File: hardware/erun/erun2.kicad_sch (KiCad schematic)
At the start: 21 parts, among them J1 Conn_Coaxial, J10 Conn_01x03_Female, J2 HEIDENHAIN_MT25_TTL, J3 TRIGGER_TTL, J4 Conn_01x02_Female, J5 Conn_01x02_Female, J6 Conn_01x02_Female, J7 Conn_01x02_Female, J8 Conn_01x02_Female, J9 Conn_01x03_Female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

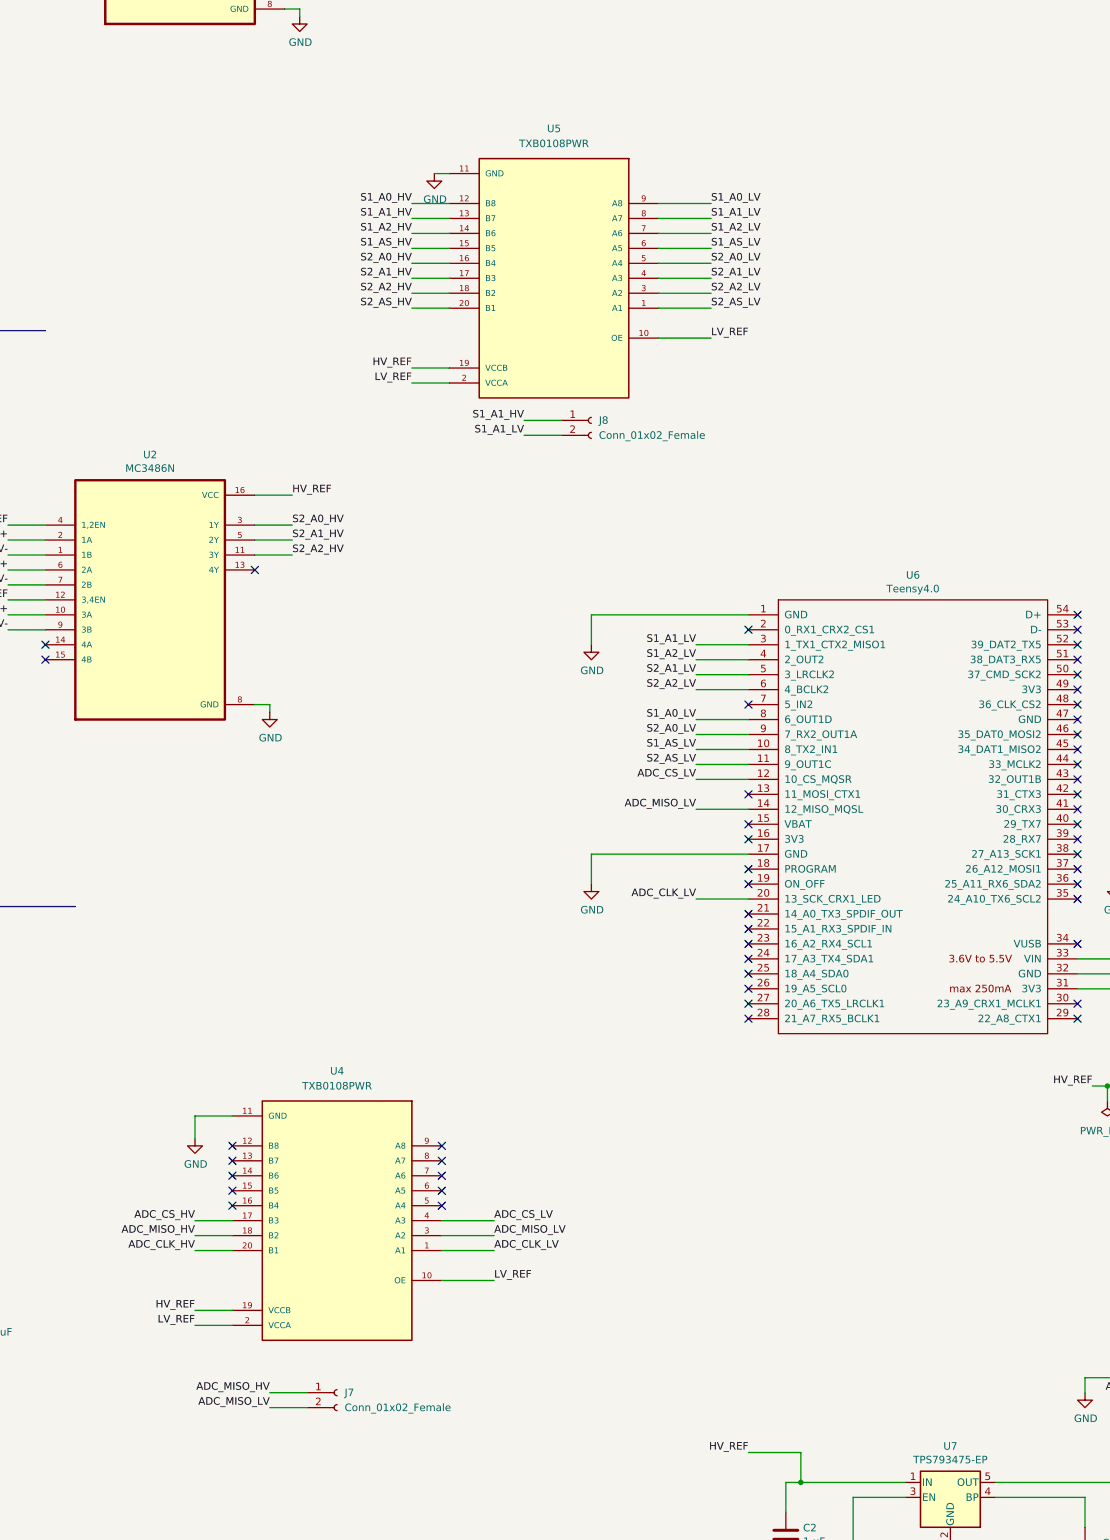
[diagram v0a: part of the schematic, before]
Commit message: Added capacitors to the board
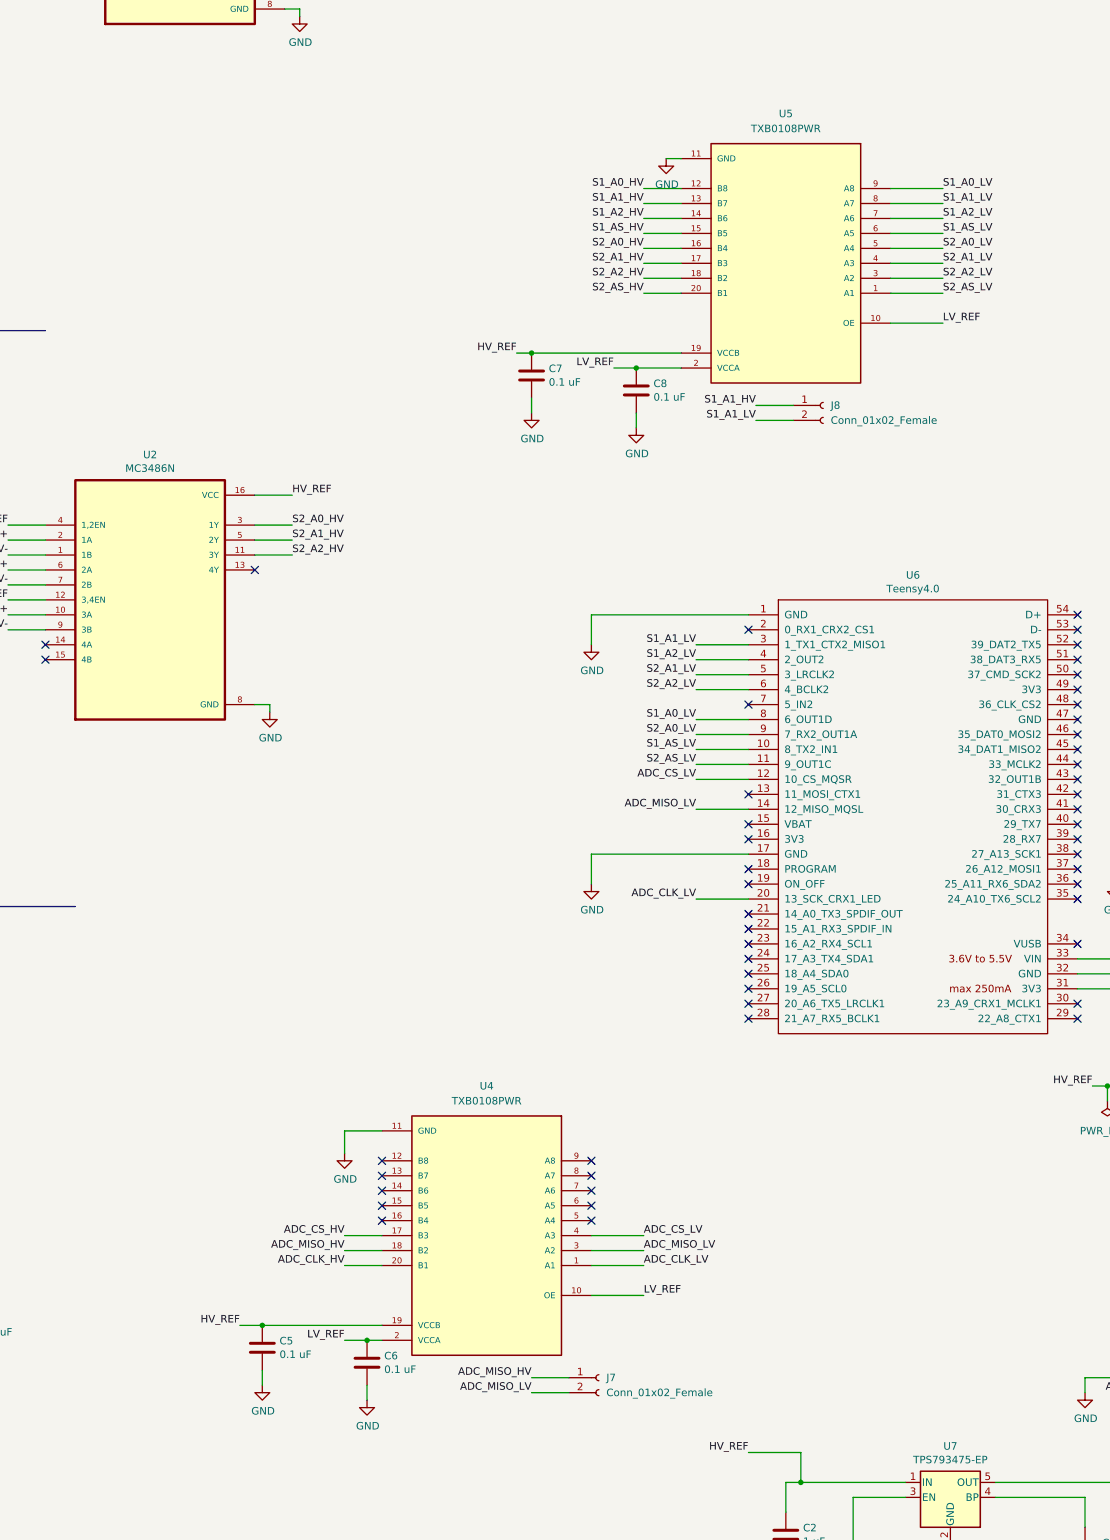
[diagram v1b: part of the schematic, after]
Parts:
- added C5, C6, C7, C8: 0.1 uF, Capacitor_SMD:C_0603_1608Metric, symbol Device:C
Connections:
- net +3V3: now also C6.1, C8.1
- net +5V: now also C5.1, C7.1
- net GND: now also C5.2, C6.2, C7.2, C8.2
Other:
- moved on the sheet: J7, J8, U4, U5

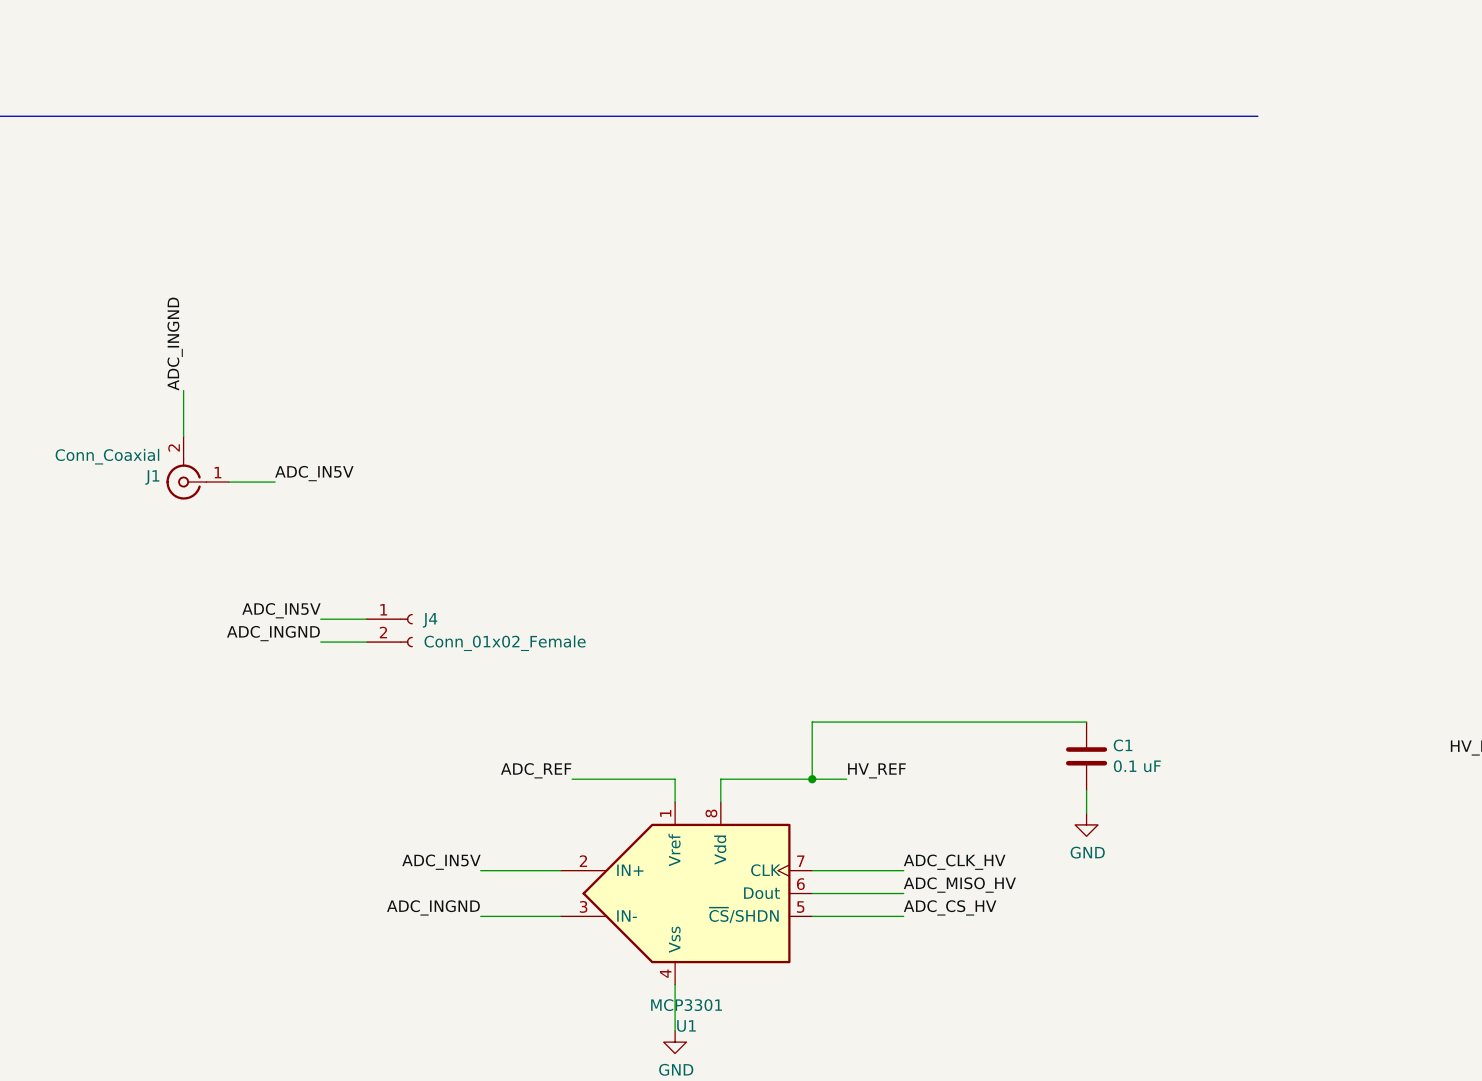
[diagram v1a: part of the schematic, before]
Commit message: Added low pass filter and minor refinements
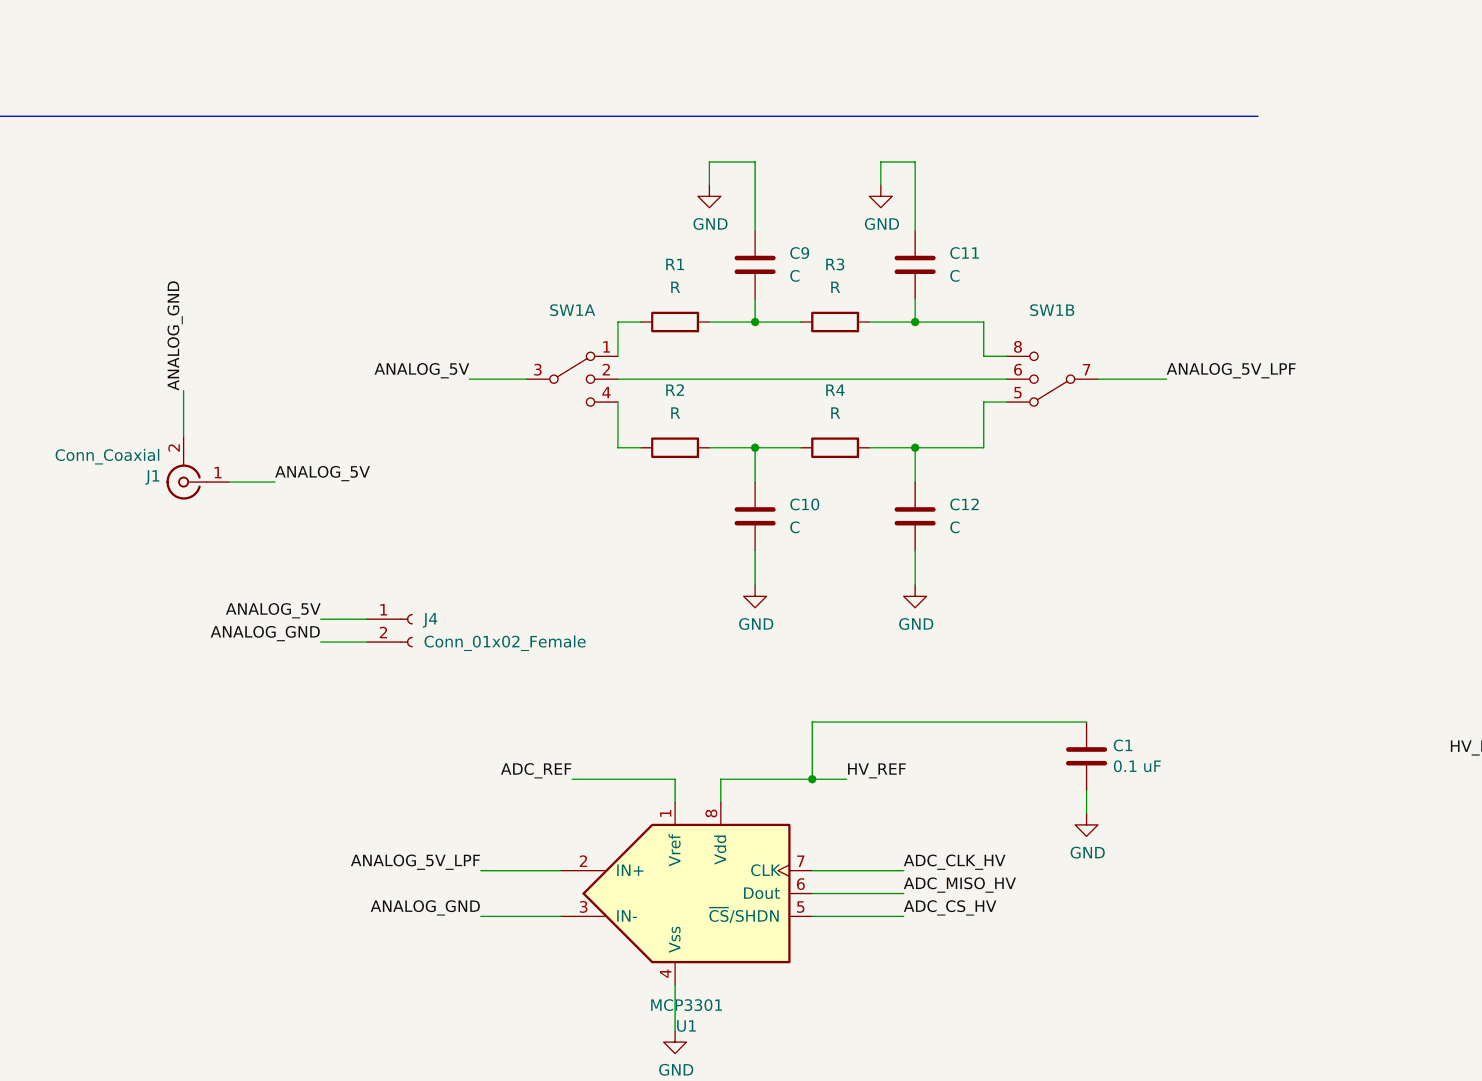
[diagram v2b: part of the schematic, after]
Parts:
- added C10, C11, C12, C9: C, Capacitor_SMD:C_0603_1608Metric, symbol Device:C
- added R1, R2, R3, R4: R, Resistor_SMD:R_0603_1608Metric, symbol Device:R
- added SW1: (no value), symbol Switch:SW_DP3T
- J1: footprint Connector_Coaxial:SMA_Amphenol_132134-14_Vertical -> Connector_Coaxial:SMA_Amphenol_132134-16_Vertical
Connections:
- net GND: now also C10.2, C11.1, C12.2, C9.1
- net ADC_IN5V renamed ANALOG_5V
- net ANALOG_5V: now also SW1.3; no longer U1.2 (IN+)
- net ADC_INGND renamed ANALOG_GND
- new net: C9.2, R1.2, R3.1
- new net: C11.2, R3.2, SW1.8
- new net: R1.1, SW1.1
- new net: C12.1, R4.2, SW1.5
- new net: SW1.2, SW1.6
- new net: R2.1, SW1.4
- new net: C10.1, R2.2, R4.1
- new net ANALOG_5V_LPF: SW1.7, U1.2 (IN+)
